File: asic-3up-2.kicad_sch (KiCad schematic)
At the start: 79 parts, among them J16 Conn_01x01, J17 Conn_01x01, J8 Conn_01x01, J9 Conn_01x01, U57 MCP1824T-1202E/OT, U58 MCP1824T-1202E/OT, U59 MCP1824T-1202E/OT, U60 MCP1824T-0802E, U61 MCP1824T-0802E, U62 MCP1824T-0802E, U63 BM1362AC_MODE1, U64 BM1362AC_MODE0, U65 BM1362AC_MODE1

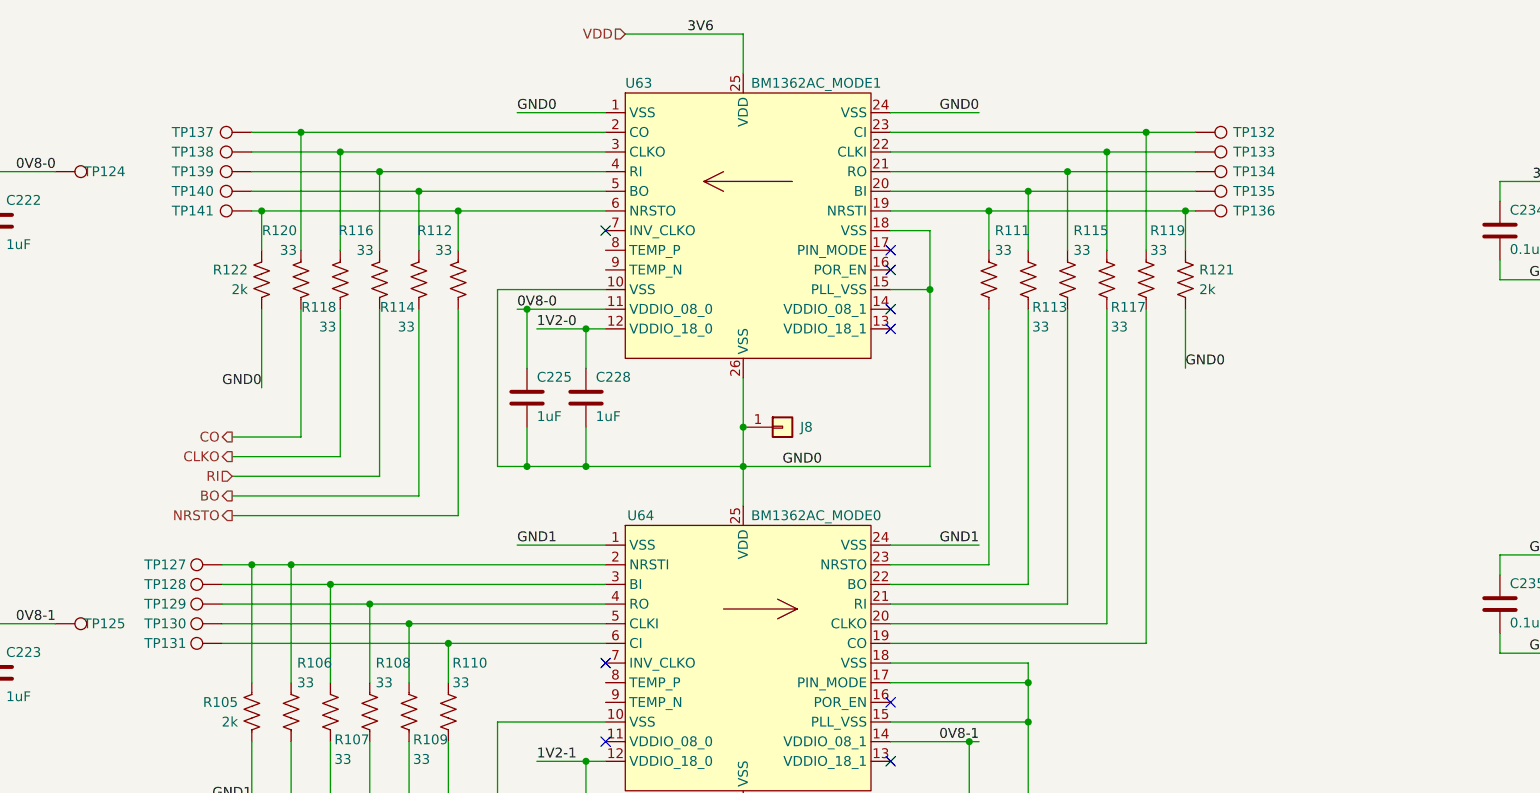
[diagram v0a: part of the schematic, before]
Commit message: all placed *almost* all routed
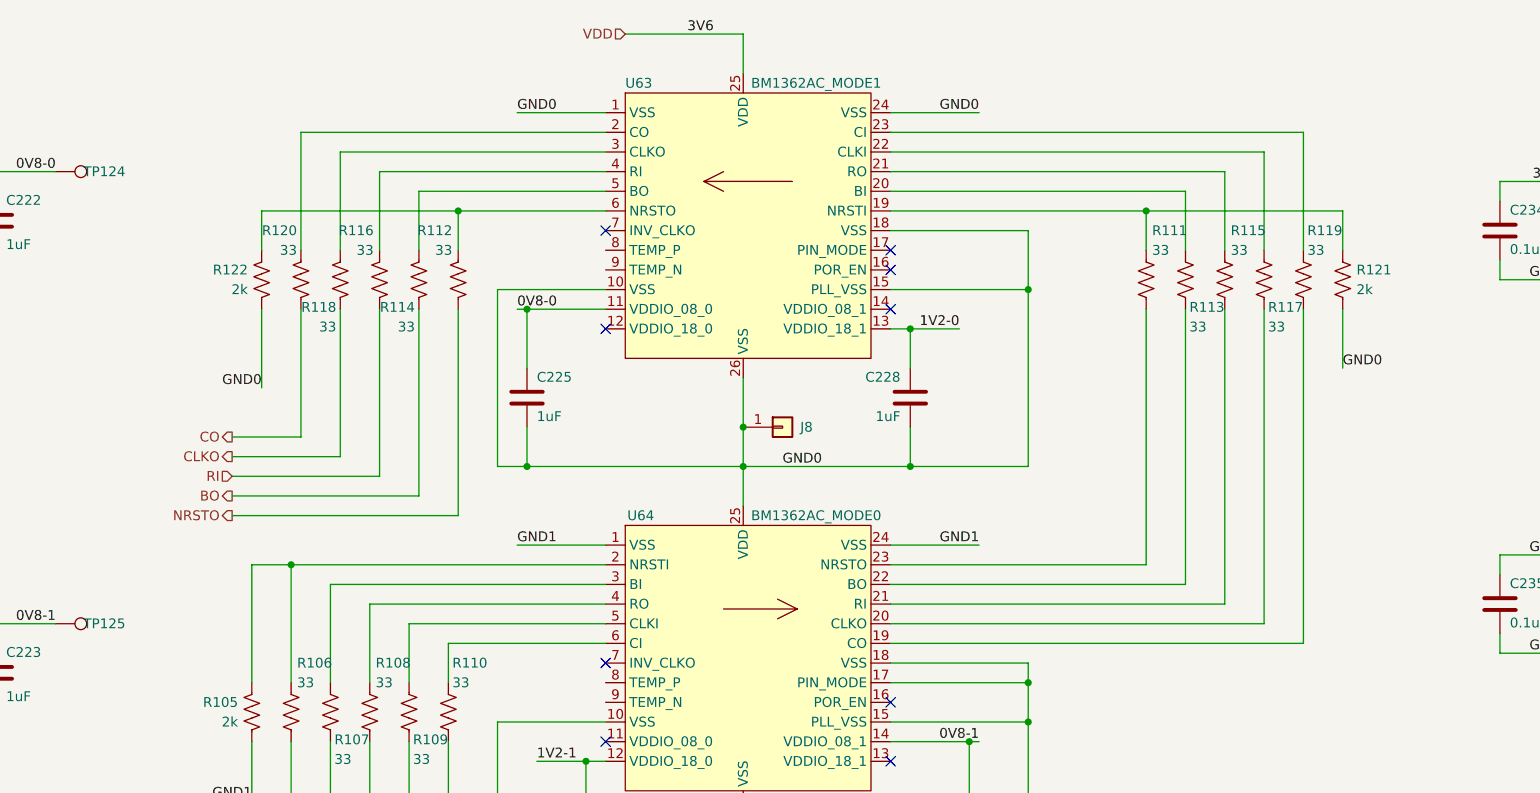
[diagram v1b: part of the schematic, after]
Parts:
- removed TP127, TP128, TP129, TP130, TP131, TP132, TP133, TP134, TP135, TP136, TP137, TP138, TP139, TP140, TP141: TestPoint, TestPoint:TestPoint_Pad_D1.0mm, symbol Connector:TestPoint
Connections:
- net 1V2-0: now also U63.13 (VDDIO_18_1); no longer U63.12 (VDDIO_18_0)
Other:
- moved on the sheet: C228, R111, R113, R115, R117, R119, R121

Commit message: changed the RP2040 Flash to a QSPI version. Added DK RP2040 crystal. Added LED. Added some 3D models. Generated BOM. Generated Gerbers
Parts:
- R105, R121, R122: DK (none) -> 311-2KLRCT-ND; PARTNO (none) -> RC0402FR-072KL
- R106, R107, R108, R109, R110, R111, R112, R113, R114, R115, R116, R117, R118, R119, R120: DK (none) -> 311-33.0LRCT-ND; PARTNO (none) -> RC0402FR-0733RL

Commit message: generated updated gerbers
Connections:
- no-connect marks 20 -> 26
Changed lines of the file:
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@@
+	)
+	(no_connect
+		(at 231.14 74.93)
 	)
 	(no_connect
@@
 	)
 	(no_connect
+		(at 231.14 130.81)
+	)
+	(no_connect
 		(at 267.97 140.97)
+	)
+	(no_connect
+		(at 231.14 189.23)
 	)
 	(no_connect
@@
 	)
 	(no_connect
+		(at 231.14 186.69)
+	)
+	(no_connect
 		(at 267.97 77.47)
 	)
@@
 	)
 	(no_connect
+		(at 231.14 133.35)
+	)
+	(no_connect
 		(at 231.14 138.43)
 	)
@@
 	(no_connect
 		(at 66.04 185.42)
+	)
+	(no_connect
+		(at 231.14 77.47)
 	)
 	(no_connect
@@
 		)
 	)
-	(label "3V6"
+	(label "VDD"
 		(at 354.33 66.04 180)
 		(fields_autoplaced yes)
@@
 		)
 	)
-	(label "3V6"
+	(label "VDD"
 		(at 245.11 46.99 180)
 		(fields_autoplaced yes)
